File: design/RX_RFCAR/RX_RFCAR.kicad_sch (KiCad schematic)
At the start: 45 parts, among them IC1 TB6612FNG, J1 V_Battery, J2 STLINK, J3 Motores, J4 BATTLEDS, J5 UART, J6 Servo_Motor, J7 NRF24L01, J8 Conn_01x03_Pin, SW1 SW_DPST_x2, U1 STM32F103C8Tx, U2 AMS1117-3.3, U3 AMS1117-3.3, U5 AMS1117-5.0, Y1 8MHz

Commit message: refactor: move design folders
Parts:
- removed C2_driver1: 0.1uF, Capacitor_SMD:C_0805_2012Metric, symbol Device:C
- removed C3_Driver1: 10uF, TAJB226K016RNJ:CAPPC3528X210N, symbol TAJB226K016RNJ:TAJB226K016RNJ
- added C2_Driver, C3_Driver: 10uF, TAJB226K016RNJ:CAPPC3528X210N, symbol TAJB226K016RNJ:TAJB226K016RNJ
- added C4_Driver: 0.1uF, Capacitor_SMD:C_0805_2012Metric, symbol Device:C
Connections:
- net 5V: no longer C16.1, C17.1, U5.2 (VO)
- net GND: now also C14.2, C15.2, C16.2, C17.2, C2_Driver.1, C3_Driver.1, C4_Driver.2
- net VCC: now also C3_Driver.2, C4_Driver.1
- net VIN: no longer C1_Driver1.1, IC1.13 (VM2), IC1.14 (VM3), IC1.24 (VM1)
- new net: C1_Driver1.1, C2_Driver.2, IC1.13 (VM2), IC1.14 (VM3), IC1.24 (VM1)
- new net +5V: C16.1, C17.1, U5.2 (VO)
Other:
- moved on the sheet: C10, C11, C12, C13, C14, C15, C16, C17, C7, C8, D1, J8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

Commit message: refactor: rearrage schematic
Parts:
- removed C3_Driver: 10uF, TAJB226K016RNJ:CAPPC3528X210N, symbol TAJB226K016RNJ:TAJB226K016RNJ
- renumbered C2_Driver to C2_Driver1, C4_Driver to C4_Driver1
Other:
- company: (none) -> Das
- moved on the sheet: C1_Driver1, C2_Driver1, C4_Driver1, C7, C8, IC1, J3, U2

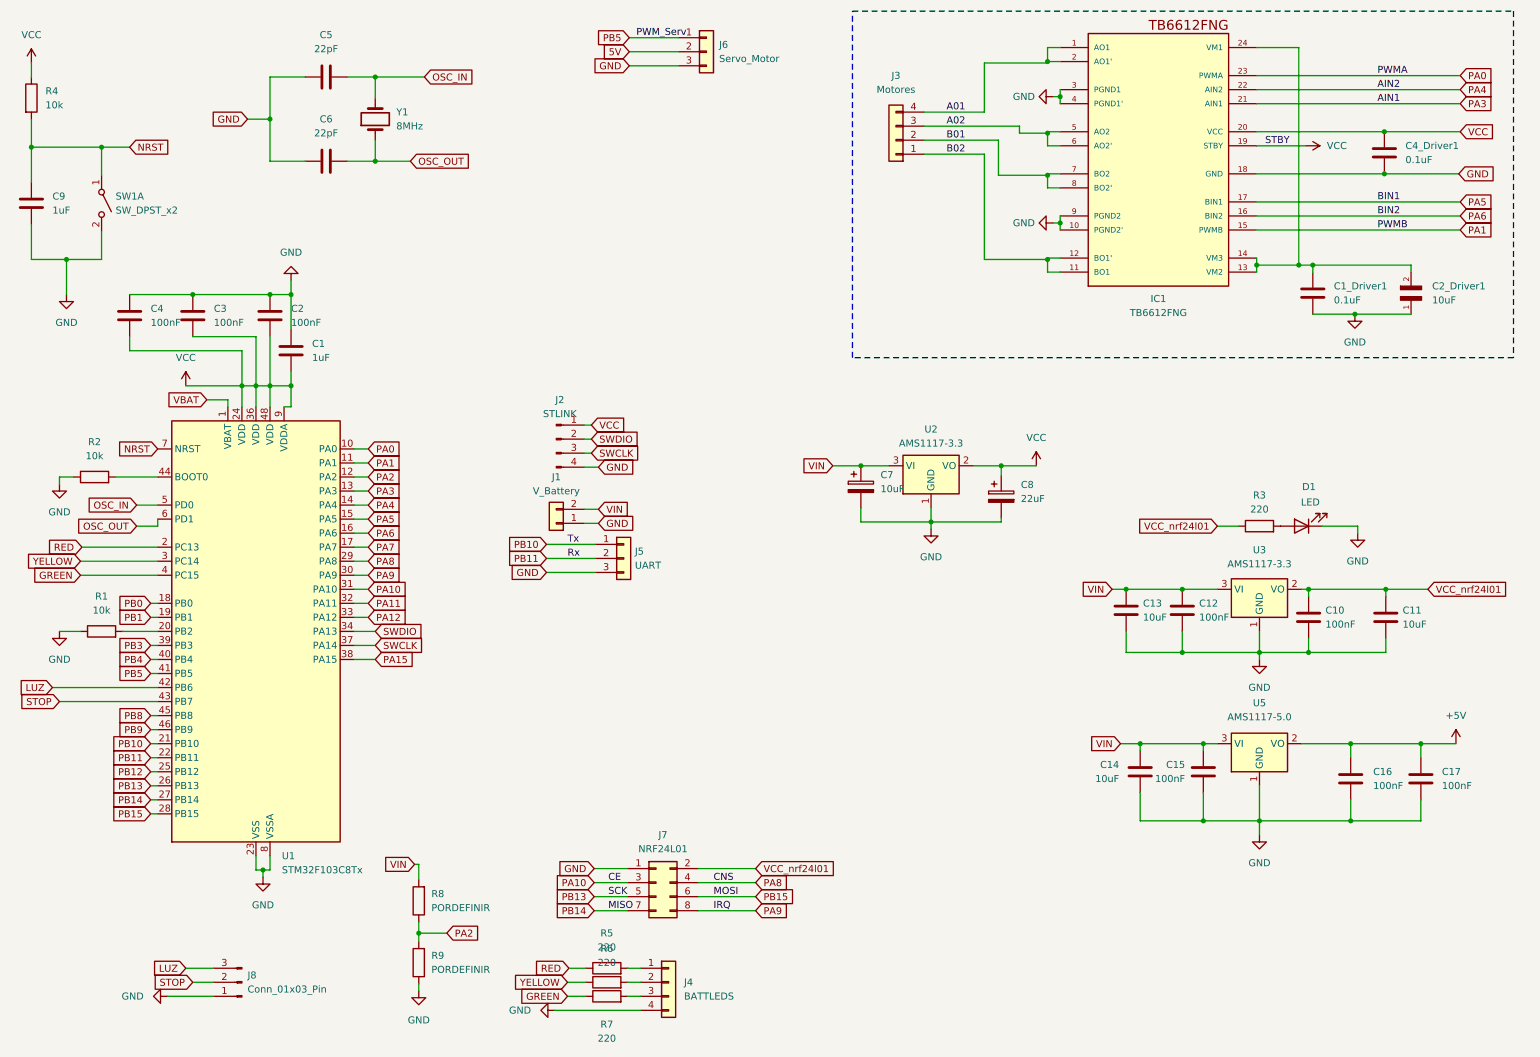
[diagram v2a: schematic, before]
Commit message: refactor: change net gnd to simbol gnd
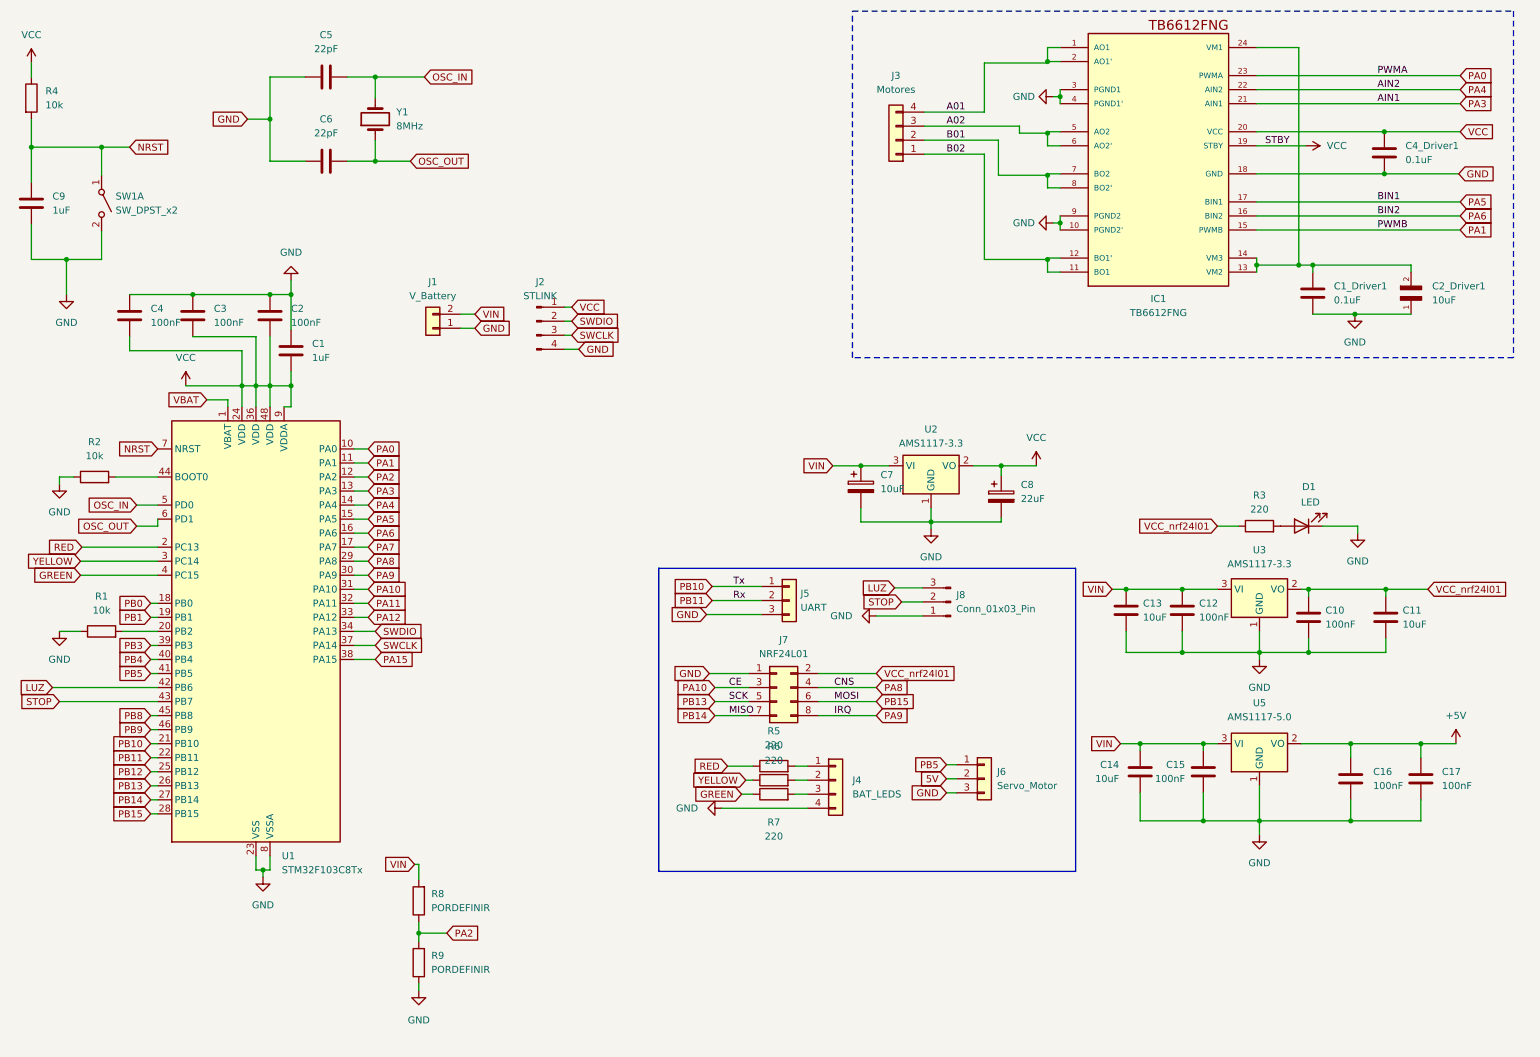
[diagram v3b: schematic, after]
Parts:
- J4: value BATTLEDS -> BAT_LEDS
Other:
- moved on the sheet: J1, J2, J4, J5, J6, J7, J8, R5, R6, R7

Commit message: fix: merge changes of Ale
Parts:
- removed J2: STLINK, Connector_PinHeader_2.54mm:PinHeader_1x04_P2.54mm_Vertical, symbol Connector:Conn_01x04_Pin
- added C19: 100n, PCM_Capacitor_SMD_AKL:C_0201_0603Metric, symbol Device:C_Small
- added J2: Conn_02x04_Odd_Even, Package_SO:SOIC-8_3.9x4.9mm_P1.27mm, symbol Connector_Generic:Conn_02x04_Odd_Even
- added J9: STLINK, Connector_PinSocket_2.54mm:PinSocket_1x01_P2.54mm_Vertical, symbol Connector_Generic:Conn_01x04
- J1: value V_Battery -> V_Bat
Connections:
- net 5V is gone; now on net +5V: J6.2 (Pin_2)
- net GND: now also C19.2, J9.4 (Pin_4)
- net SWCLK: now also J9.3 (Pin_3)
- net SWDIO: now also J9.2 (Pin_2)
- net VCC: now also C19.1, J9.1 (Pin_1)
- net VIN renamed +BATT
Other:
- moved on the sheet: J1, R8, R9

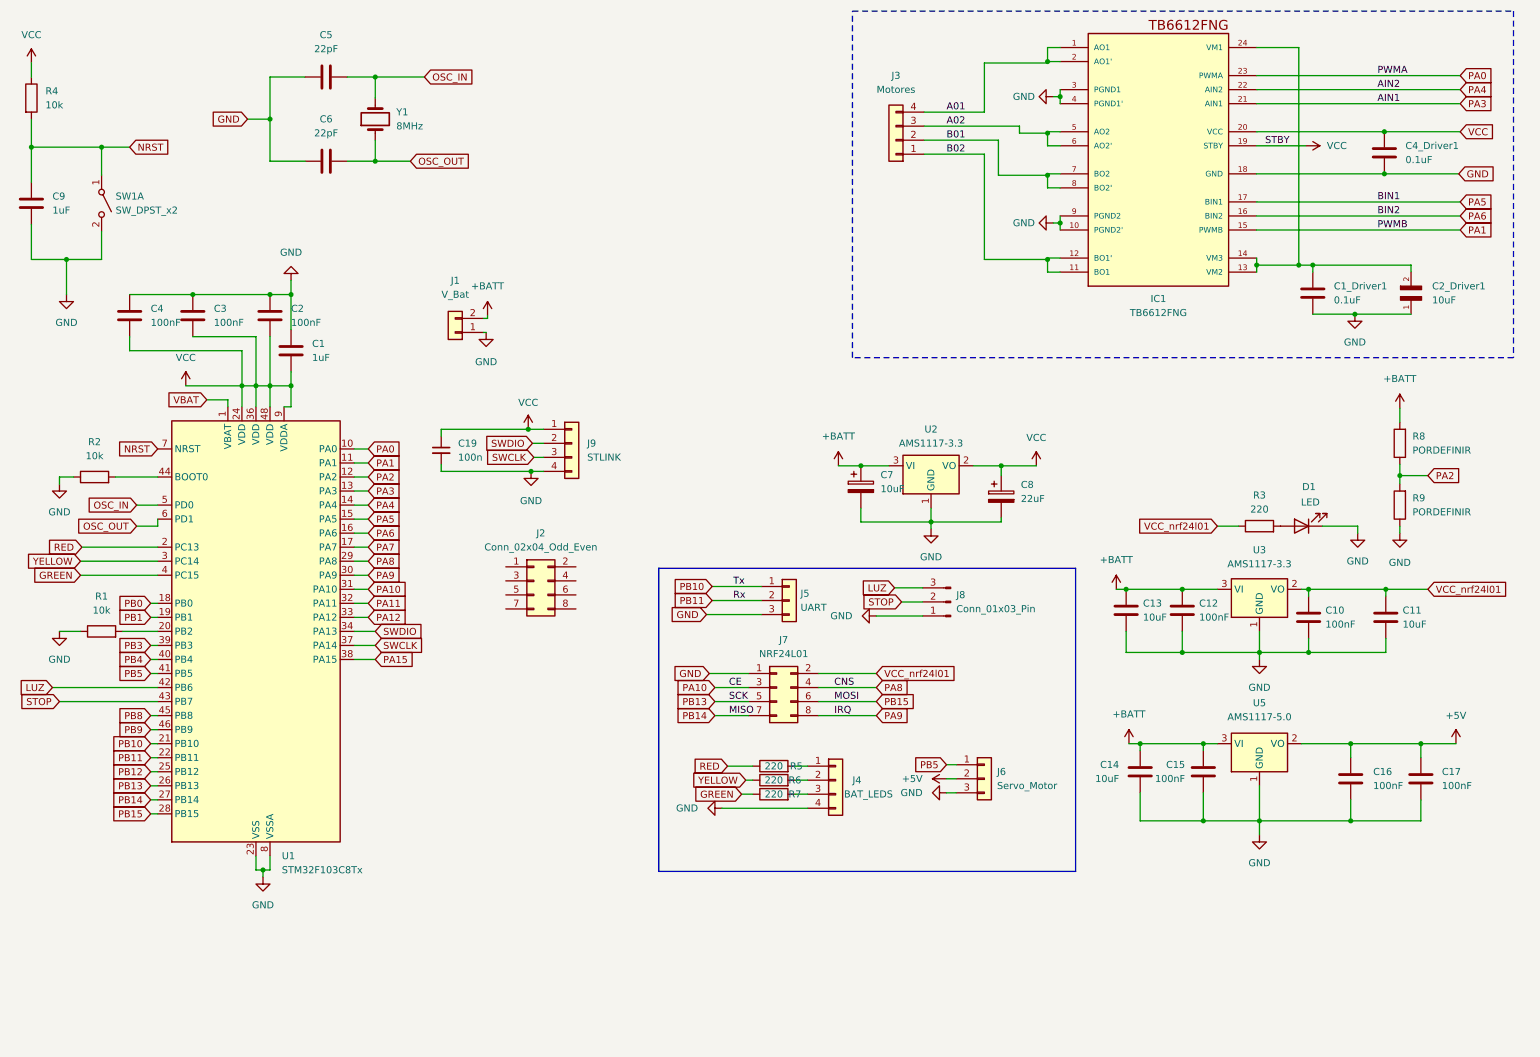
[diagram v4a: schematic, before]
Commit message: refactor: change net gnd to simbol gnd
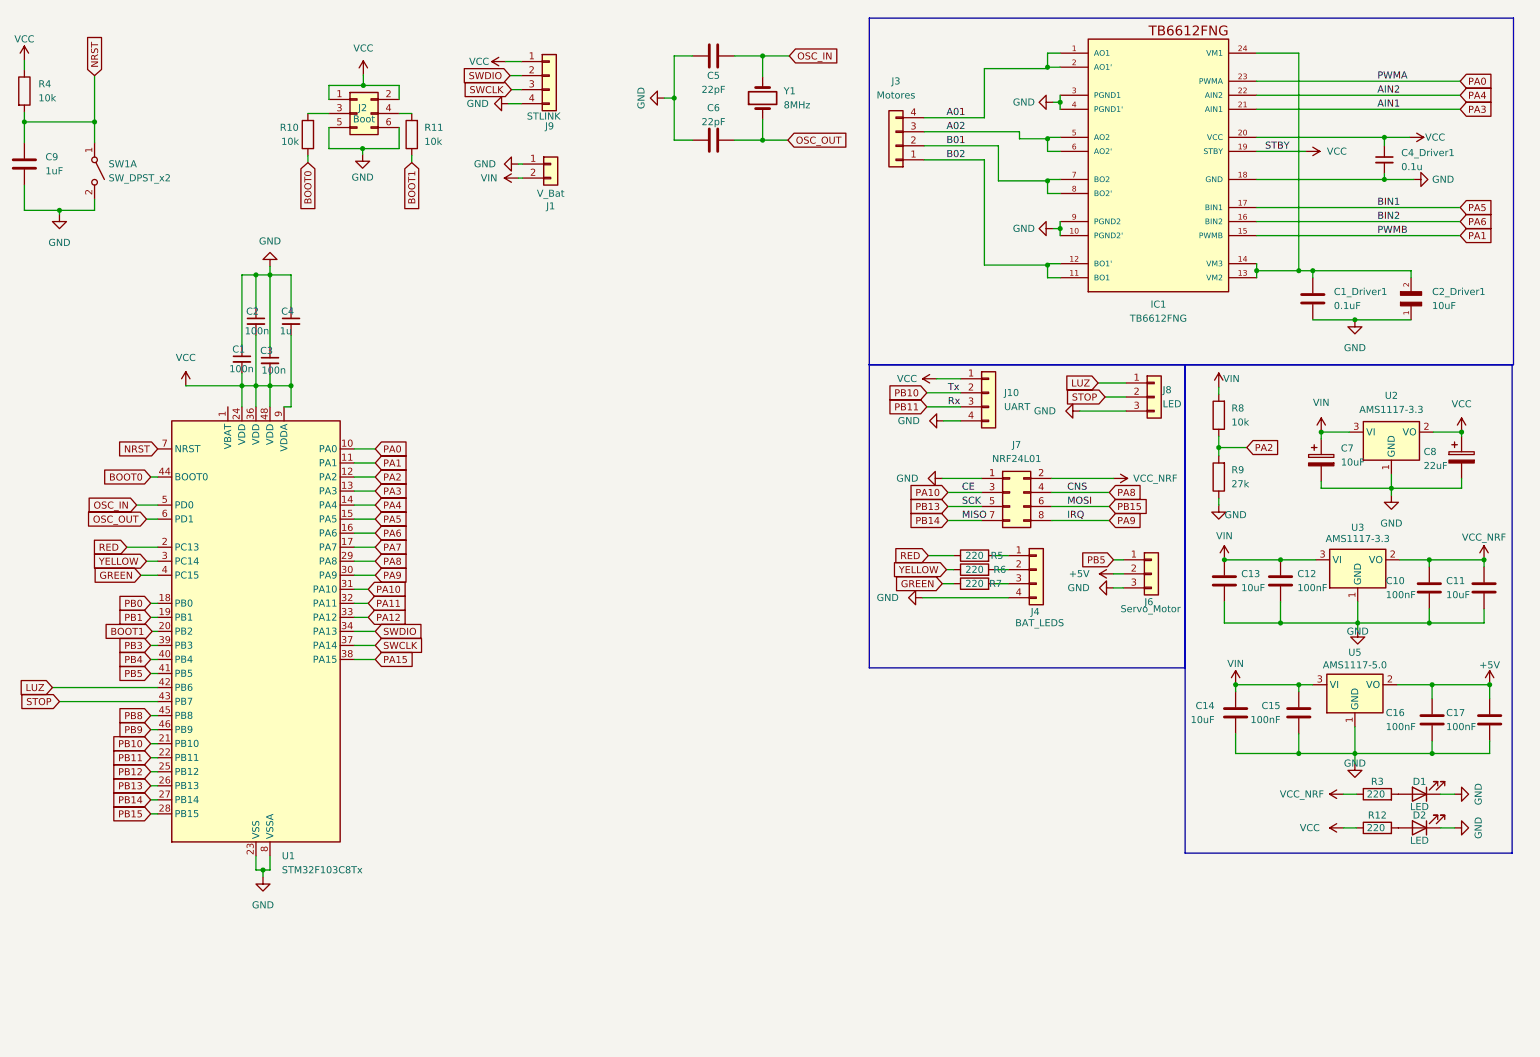
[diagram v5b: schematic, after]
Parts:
- removed C1: 1uF, Capacitor_SMD:C_0805_2012Metric, symbol Device:C
- removed C19: 100n, PCM_Capacitor_SMD_AKL:C_0201_0603Metric, symbol Device:C_Small
- removed C2, C3, C4: 100nF, Capacitor_SMD:C_0805_2012Metric_Pad1.18x1.45mm_HandSolder, symbol Device:C
- removed C4_Driver1: 0.1uF, Capacitor_SMD:C_0805_2012Metric, symbol Device:C
- removed J2: Conn_02x04_Odd_Even, Package_SO:SOIC-8_3.9x4.9mm_P1.27mm, symbol Connector_Generic:Conn_02x04_Odd_Even
- removed J5: UART, Connector_PinHeader_2.54mm:PinHeader_1x03_P2.54mm_Vertical, symbol Connector_Generic:Conn_01x03
- removed J8: Conn_01x03_Pin, Connector_PinHeader_2.54mm:PinHeader_1x03_P2.54mm_Vertical, symbol Connector:Conn_01x03_Pin
- removed R1, R2: 10k, Resistor_SMD:R_0805_2012Metric, symbol Device:R
- added C1, C2, C3: 100n, PCM_Capacitor_SMD_AKL:C_0201_0603Metric, symbol Device:C_Small
- added C4: 1u, PCM_Capacitor_SMD_AKL:C_0201_0603Metric, symbol Device:C_Small
- added C4_Driver1: 0.1u, symbol Device:C_Small
- added D2: LED, LED_SMD:LED_0603_1608Metric, symbol Device:LED
- added J10: UART, PCM_SL_Connectors:PinHeader_1x06_P2.54mm_Vertical, symbol Connector_Generic:Conn_01x04
- added J2: Boot, symbol Connector_Generic:Conn_02x03_Odd_Even
- added J8: LED, Connector_PinHeader_2.54mm:PinHeader_1x03_P2.54mm_Vertical, symbol Connector_Generic:Conn_01x03
- added R10, R11: 10k, Resistor_SMD:R_0805_2012Metric, symbol Device:R
- added R12: 220, Resistor_SMD:R_0805_2012Metric, symbol Device:R
- R8: value PORDEFINIR -> 10k
- R9: value PORDEFINIR -> 27k
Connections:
- net GND: now also C1.1, C2.1, C3.1, C4.1, C4_Driver1.2, D2.1 (K), J10.4 (Pin_4), J2.5 (Pin_5), J2.6 (Pin_6), J8.3 (Pin_3)
- net LUZ: now also J8.1 (Pin_1)
- net PB10: now also J10.2 (Pin_2)
- net PB11: now also J10.3 (Pin_3)
- net STOP: now also J8.2 (Pin_2)
- net VCC: now also C1.2, C2.2, C3.2, C4.2, C4_Driver1.1, J10.1 (Pin_1), J2.1 (Pin_1), J2.2 (Pin_2), R12.1
- net BOOT1: now reaches U1.20 (PB2)
- net BOOT1: now also R11.1
- net BOOT0: now reaches U1.44 (BOOT0)
- net BOOT0: now also R10.1
- net +BATT renamed VIN
- net VBAT: no longer names the net of U1.1 (VBAT)
- net VCC_nrf24l01 renamed VCC_NRF
- new net: D2.2 (A), R12.2
- new net: J2.4 (Pin_4), R11.2
- new net: J2.3 (Pin_3), R10.2
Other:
- company: Das -> Das Reyxr
- title: (none) -> RX_RFCar
- moved on the sheet: C10, C11, C12, C13, C14, C15, C16, C17, C1_Driver1, C2_Driver1, C5, C6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
